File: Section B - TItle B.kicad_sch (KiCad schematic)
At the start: 79 parts, among them IC1 MAX232EIDR, J1 Power, J2 Analog, J3 Analog, J4 Digital, J6 PWM, J7 PWM, J8 Communication, J9 Conn_01x06, Q13 IRLML2060, Q22 IRLML2060, Q4 IRLML2060, T15 TestPoint, T16 TestPoint, T17 TestPoint, T18 TestPoint, T19 TestPoint, T20 TestPoint, T21 TestPoint, T22 TestPoint, T23 TestPoint, T24 TestPoint, T25 TestPoint, T26 TestPoint, T27 TestPoint, T28 TestPoint, T29 TestPoint, T30 TestPoint, T31 TestPoint, T32 TestPoint, T33 TestPoint, T34 TestPoint, T35 TestPoint, T36 TestPoint, T37 TestPoint, T38 TestPoint

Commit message: PCB Preliminary version
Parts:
- added T11, T12, T13: TestPoint, TestPoint:TestPoint_Pad_1.0x1.0mm, symbol Connector:TestPoint
- T15, T16, T17, T18, T19, T20, T21, T22, T23, T24, T25, T26, T27, T28, T29, T30, T31, T32, T33, T34, T35, T36, T37, T38: footprint SamacSys_Parts:TestPoint_Pad_0.6x0.6mm -> TestPoint:TestPoint_Pad_1.0x1.0mm
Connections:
- net A: no longer names the net of J7.5 (Pin_5)
- net A: now also T11.1
- net B: no longer names the net of J7.6 (Pin_6)
- net B: now also T12.1
- net C: no longer names the net of J4.33 (Pin_33)
- net C: now also T13.1
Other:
- note added: "RX3/15"
- note added: "TX3/14"
- moved on the sheet: C3, C4, C5, C6, C7, DL1, DL2, DL3, DL4, DL5, DL6, DL7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

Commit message: PCB Checked version
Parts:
- IC1: footprint SOIC127P600X175-16N -> SamacSys_Parts:SOIC127P600X175-16N
- J1, J2, J3, J7, J8: Realtra Part Number (none) -> R-CON-1268-SHV8
- J4: Realtra Part Number (none) -> R-CON-1270-2RVH
- J6: Realtra Part Number (none) -> R-CON-1269-SH12
- J9: Manufacturer (none) -> WURTH ELEKTRONIK; Manufacturer Part Number (none) -> 61300811121; Realtra Part Number (none) -> R-CON-1268-SHV8
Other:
- title: Sheet Title B -> Arduino Mega 2560

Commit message: Schematic and PCB update
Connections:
- net Ardu_RX renamed ARDU_UART_RX
- net ARDU_UART_RX: now also IC1.9 (ROUT2); no longer IC1.10 (DIN2)
- net RX renamed RS232_RX_IN
- net TX renamed RS232_TX_OUT
- net TX3/14 renamed ARDU_UART_TX
- net ARDU_UART_TX: now also IC1.10 (DIN2); no longer IC1.9 (ROUT2)
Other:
- note added: "Arduino Mega 2560"
- note added: "From PDCU"
- note removed: "Flexible I/O source configuration"
- note removed: "Flexible I/O worked examples"
- note removed: "From VDCU"
- note removed: "References:"
- moved on the sheet: C4, R56, R57

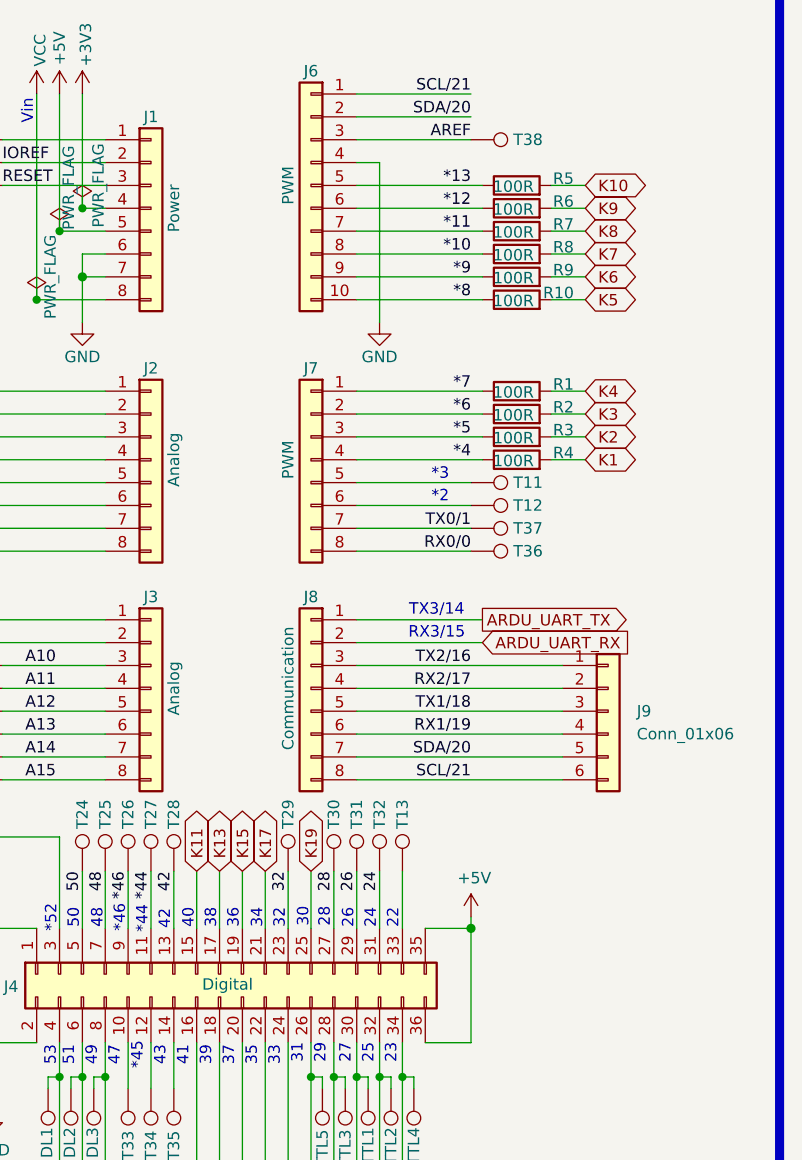
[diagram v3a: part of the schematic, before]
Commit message: created for the Realtra part number
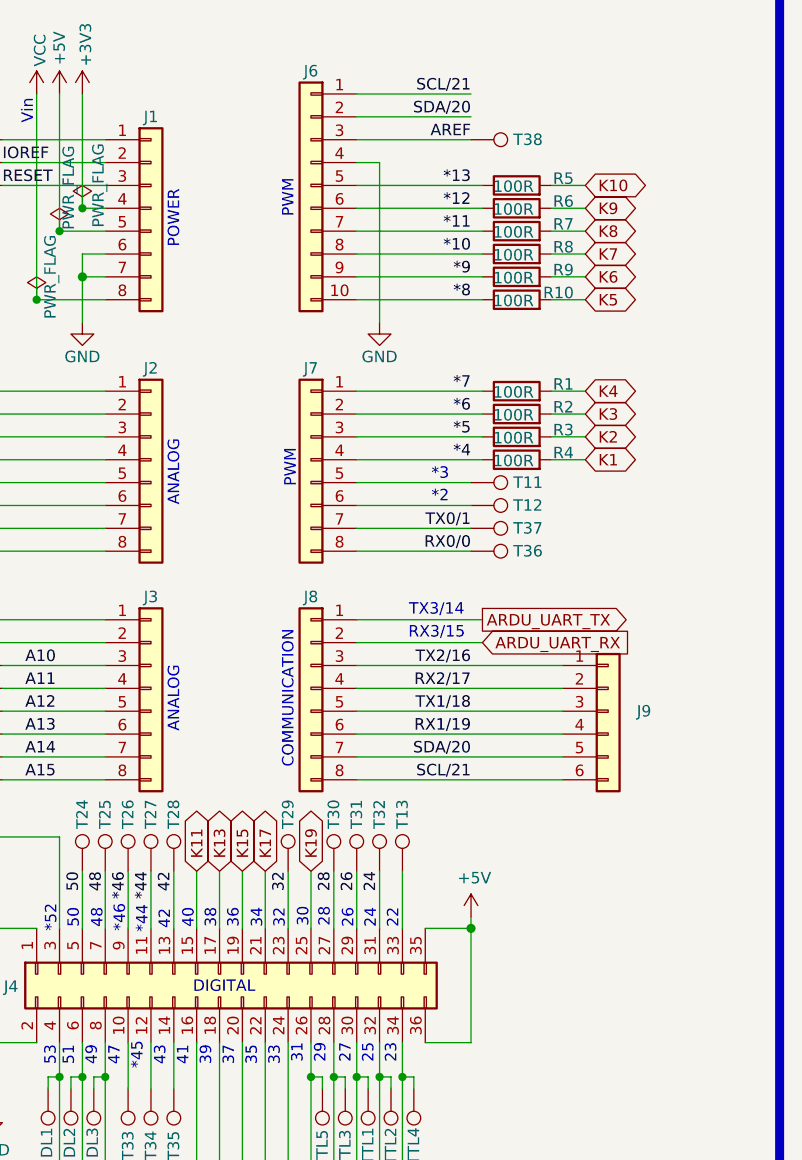
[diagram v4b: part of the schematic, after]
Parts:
- J1: value Power -> 61300811121
- J2, J3: value Analog -> 61300811121
- J4: value Digital -> 61304021121
- J6: value PWM -> 61301211121
- J7: value PWM -> 61300811121
- J8: value Communication -> 61300811121
- J9: value Conn_01x06 -> 61300811121
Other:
- note added: "ANALOG"
- note added: "COMMUNICATION"
- note added: "DIGITAL"
- note added: "POWER"
- note added: "PWM"
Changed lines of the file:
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@@
 		)
 	)
+	(text "PWM"
+		(exclude_from_sim no)
+		(at 265.684 107.696 90)
+		(effects
+			(font
+				(size 1.27 1.27)
+			)
+		)
+	)
 	(text "*44"
 		(exclude_from_sim no)
@@
 		)
 	)
+	(text "COMMUNICATION"
+		(exclude_from_sim no)
+		(at 265.43 133.35 90)
+		(effects
+			(font
+				(size 1.27 1.27)
+			)
+		)
+	)
 	(text "38"
 		(exclude_from_sim no)
@@
 		)
 	)
+	(text "ANALOG"
+		(exclude_from_sim no)
+		(at 252.73 133.35 90)
+		(effects
+			(font
+				(size 1.27 1.27)
+			)
+		)
+	)
 	(text "From PDCU"
 		(exclude_from_sim no)
@@
 		)
 	)
+	(text "PWM"
+		(exclude_from_sim no)
+		(at 265.43 77.724 90)
+		(effects
+			(font
+				(size 1.27 1.27)
+			)
+		)
+	)
 	(text "51"
 		(exclude_from_sim no)
@@
 		)
 	)
+	(text "DIGITAL"
+		(exclude_from_sim no)
+		(at 258.318 165.354 0)
+		(effects
+			(font
+				(size 1.27 1.27)
+			)
+		)
+	)
 	(text "A8"
 		(exclude_from_sim no)
@@
 		)
 	)
+	(text "ANALOG"
+		(exclude_from_sim no)
+		(at 252.73 108.204 90)
+		(effects
+			(font
+				(size 1.27 1.27)
+			)
+		)
+	)
 	(text "33"
 		(exclude_from_sim no)
@@
 		)
 	)
+	(text "POWER"
+		(exclude_from_sim no)
+		(at 252.73 80.01 90)
+		(effects
+			(font
+				(size 1.27 1.27)
+			)
+		)
+	)
 	(text_box "LAYOUT NOTE:\nAdd more vias to the 28V, VTX1, and the other three high-current (up to 3A) nets, and increase the trace width accordingly."
 		(exclude_from_sim no)
@@
 			)
 		)
-		(property "Value" "Power"
+		(property "Value" "61300811121"
 			(at 252.73 78.74 90)
 			(effects
@@
 					(size 1.27 1.27)
 				)
+				(hide yes)
 			)
 		)
@@
 			)
 		)
-		(property "Value" "PWM"
+		(property "Value" "61301211121"
 			(at 265.43 76.2 90)
 			(effects
@@
 					(size 1.27 1.27)
 				)
+				(hide yes)
 			)
 		)
@@
 			)
 		)
-		(property "Value" "Analog"
+		(property "Value" "61300811121"
 			(at 252.73 106.68 90)
 			(effects
@@
 					(size 1.27 1.27)
 				)
+				(hide yes)
 			)
 		)
@@
 			)
 		)
-		(property "Value" "PWM"
+		(property "Value" "61300811121"
 			(at 265.43 106.68 90)
 			(effects
@@
 					(size 1.27 1.27)
 				)
+				(hide yes)
 			)
 		)
@@
 			)
 		)
-		(property "Value" "Analog"
+		(property "Value" "61300811121"
 			(at 252.73 132.08 90)
 			(effects
@@
 					(size 1.27 1.27)
 				)
+				(hide yes)
 			)
 		)
@@
 			)
 		)
-		(property "Value" "Communication"
+		(property "Value" "61300811121"
 			(at 265.43 132.08 90)
 			(effects
@@
 					(size 1.27 1.27)
 				)
+				(hide yes)
 			)
 		)
@@
 			)
 		)
-		(property "Value" "Digital"
+		(property "Value" "61304021121"
 			(at 258.699 164.973 90)
 			(effects
@@
 					(size 1.27 1.27)
 				)
+				(hide yes)
 			)
 		)
@@
 			)
 		)
-		(property "Datasheet" "~"
+		(property "Datasheet" "https://www.vishay.com/docs/20043/crcwhpe3.pdf"
 			(at 290.83 78.74 0)
 			(effects
@@
 			)
 		)
-		(property "Datasheet" "~"
+		(property "Datasheet" "https://www.vishay.com/docs/20043/crcwhpe3.pdf"
 			(at 290.83 106.68 0)
 			(effects
@@
 			)
 		)
-		(property "Datasheet" "~"
+		(property "Datasheet" "https://www.vishay.com/docs/20043/crcwhpe3.pdf"
 			(at 290.83 104.14 0)
 			(effects
@@
 			)
 		)
-		(property "Datasheet" "~"
+		(property "Datasheet" "https://www.vishay.com/docs/20043/crcwhpe3.pdf"
 			(at 290.83 101.6 0)
 			(effects
@@
 			)
 		)
-		(property "Datasheet" "~"
+		(property "Datasheet" "https://www.vishay.com/docs/20043/crcwhpe3.pdf"
 			(at 290.83 76.2 0)
 			(effects
@@
 			)
 		)
-		(property "Datasheet" "~"
+		(property "Datasheet" "https://www.vishay.com/docs/20043/crcwhpe3.pdf"
 			(at 290.83 88.9 0)
 			(effects
@@
 			)
 		)
-		(property "Datasheet" "~"
+		(property "Datasheet" "https://www.vishay.com/docs/20043/crcwhpe3.pdf"
 			(at 290.83 83.82 0)
 			(effects
@@
 			)
 		)
-		(property "Datasheet" "~"
+		(property "Datasheet" "https://www.vishay.com/docs/20043/crcwhpe3.pdf"
 			(at 290.83 86.36 0)
 			(effects
@@
 			)
 		)
-		(property "Value" "Conn_01x06"
+		(property "Value" "61300811121"
 			(at 304.165 137.16 0)
 			(effects
@@
 				)
 				(justify left)
+				(hide yes)
 			)
 		)
@@
 			)
 		)
-		(property "Datasheet" "~"
+		(property "Datasheet" "https://www.vishay.com/docs/20043/crcwhpe3.pdf"
 			(at 290.83 99.06 0)
 			(effects
@@
 			)
 		)
-		(property "Datasheet" "~"
+		(property "Datasheet" "https://www.vishay.com/docs/20043/crcwhpe3.pdf"
 			(at 290.83 81.28 0)
 			(effects
